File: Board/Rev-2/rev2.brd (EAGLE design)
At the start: 150.6 x 63.2 mm, 52 parts, among them IC1 74HC595N, T1 2N3904, T2 2N3904, T3 2N3904, T4 2N3904, T5 2N3904, T6 2N3904, T7 2N3904, T8 2N3904

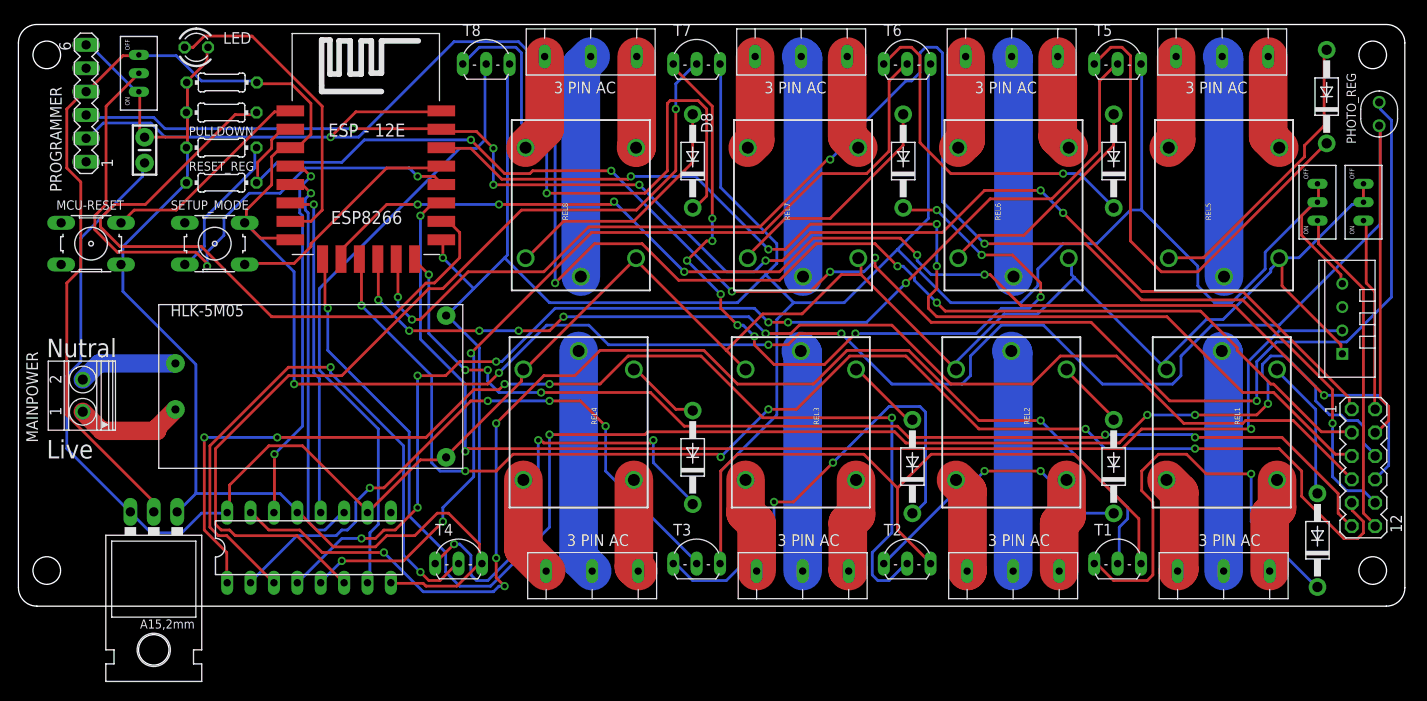
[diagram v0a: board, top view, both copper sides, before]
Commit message: Eagle Design Updated
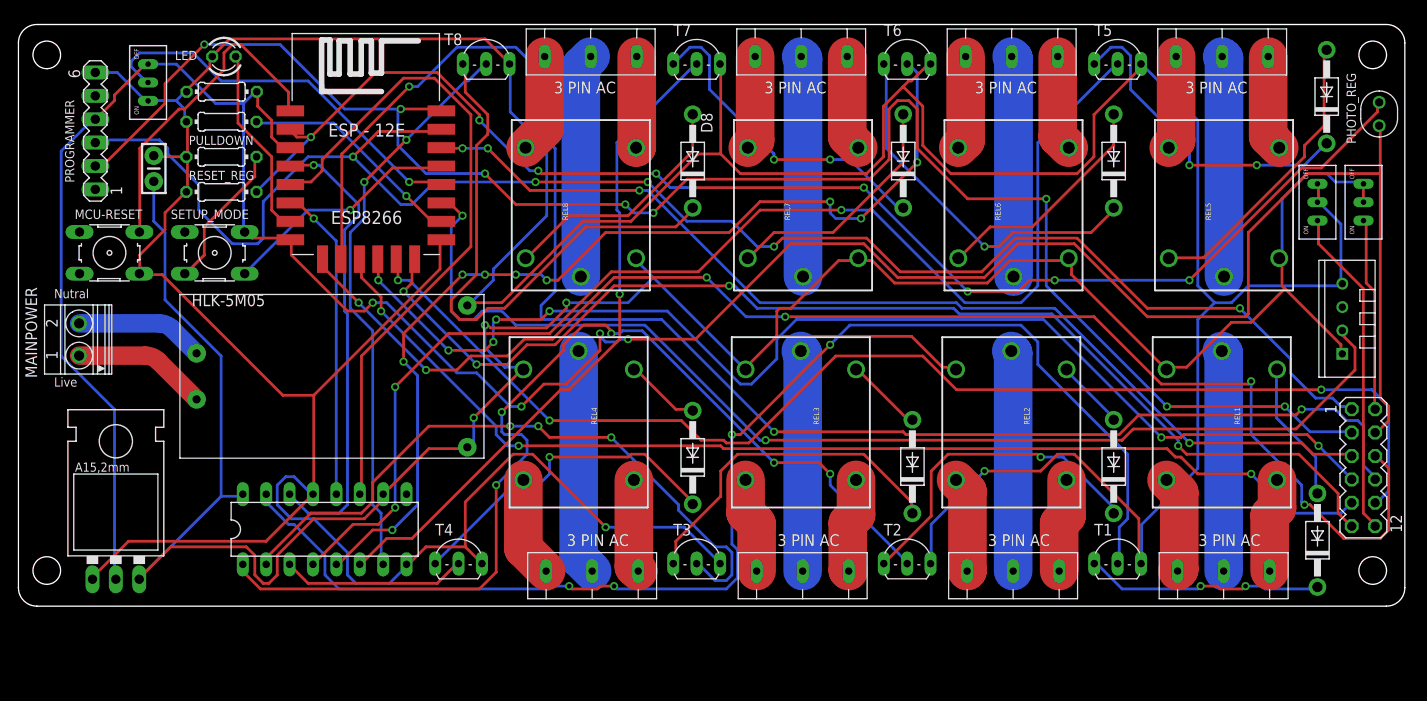
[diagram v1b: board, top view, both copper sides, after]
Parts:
- moved U$1 11.2 mm to (10.5, 11.8), turned to 0 degrees
- moved MAINPOWER 6.11 mm to (6.42, 28.9)
- moved LED 3.16 mm to (22.2, 59.7), turned to 180 degrees
- moved PROGRAMMER 3.16 mm to (8.28, 51.6)
- moved IC1 2.62 mm to (33.2, 8.31)
- moved HLK-5M05 2.55 mm to (34.0, 24.9)
- moved C1 2.24 mm to (14.6, 47.5)
- moved MCU-RESET 2.24 mm to (9.82, 38.3)
- moved FLASH 1.41 mm to (14.0, 54.8)
- moved PULLDOWN 1.00 mm to (22.0, 48.8)
- moved PULLUP 1.00 mm to (22.0, 55.8)
- moved REG1 1.00 mm to (22.0, 52.6)
- moved RESET_REG 1.00 mm to (22.0, 45.0)
- moved SETUP_MODE 1.00 mm to (21.2, 38.3)
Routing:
- net N$52: track 92.1 -> 35.5 mm, vias 10 -> 2
- net N$27: track 73.6 -> 24.6 mm, vias 0 -> 1
- net RELAY4: track 66.5 -> 20.1 mm, vias 2 -> 0
- net VCC: track 252.4 -> 287.7 mm, vias 0 -> 3
- net MISO: track 138.0 -> 169.6 mm, vias 7 -> 3
- net SHCP: track 43.7 -> 73.1 mm, vias 1 -> 0
- net ADC: track 177.6 -> 149.2 mm, vias 6 -> 9
- net RELAY7: track 99.9 -> 72.0 mm
- net MOSI: track 161.1 -> 134.6 mm, vias 5 -> 3
- net GPIO9: track 146.2 -> 122.1 mm, vias 6 -> 3
- net N$28: track 65.6 -> 43.1 mm, vias 2 -> 1
- net N$47: track 48.0 -> 26.0 mm, vias 1 -> 2
- net GND: track 491.7 -> 511.9 mm, vias 1 -> 2
- net N$5: track 53.6 -> 35.5 mm, vias 0 -> 2
- net TX: track 161.0 -> 178.4 mm, vias 7 -> 5
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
